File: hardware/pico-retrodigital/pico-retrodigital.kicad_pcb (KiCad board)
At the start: 2 copper layers, 50 x 38 mm, 70 parts, among them J1 Conn_02x05_Top_Bottom, J3 Conn_01x14, J4 Conn_01x02_Pin, J5 USB_C_Plug_USB2.0, U1 SN74LVC1G17DBVR, U2 SN74LVC1G17DBVR, U3 RP2354B, U4 SN74LVC245APW, U5 SN74LVC245APW, U6 SN74LVC245APW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

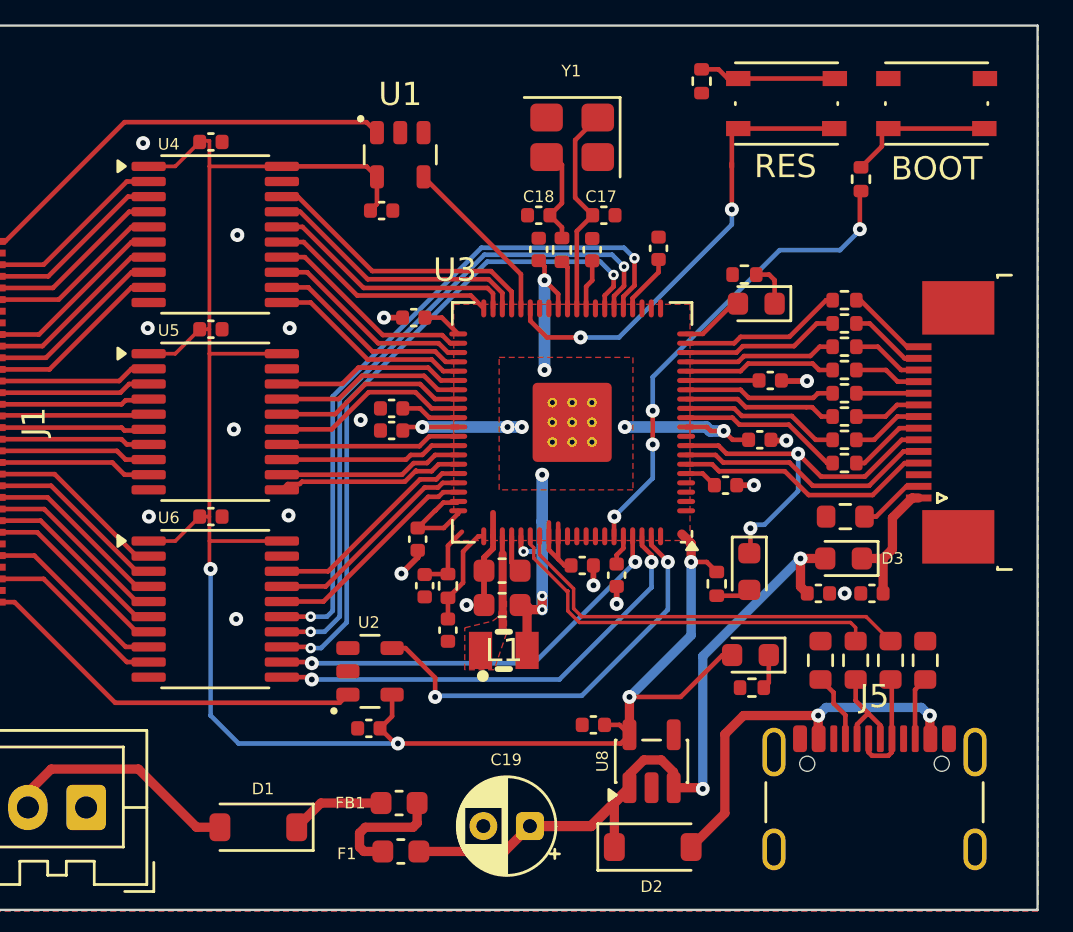
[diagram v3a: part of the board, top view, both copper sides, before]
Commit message: Clean up PCB DRC: thermal reliefs, via drills, small-via rule
- Bump all 0.6 mm vias to 0.3 mm drill (was 0.25); leave 9 small
  0.45/0.2 vias on +1V1 and CTL_0..2 untouched for tight routing
- Update Default netclass via_drill to 0.3
- Shrink thermal_bridge_width on both GND zones to 0.25 mm
- Switch U3 GND (pads 62, 81) and +1V1 (pads 10, 32, 51, 65) to
  solid zone connection for better grounding/heat dissipation
- Drop min_resolved_spokes from 2 to 1 (single-spoke thermals are
  electrically fine for reflow-assembled boards)
- Add .kicad_dru with a scoped exception allowing 0.45/0.2 vias only
  on +1V1, CTL_0, CTL_1, CTL_2 — other nets still require 0.5/0.3
- Ignore *_drc_violations.json (DRC runtime output)
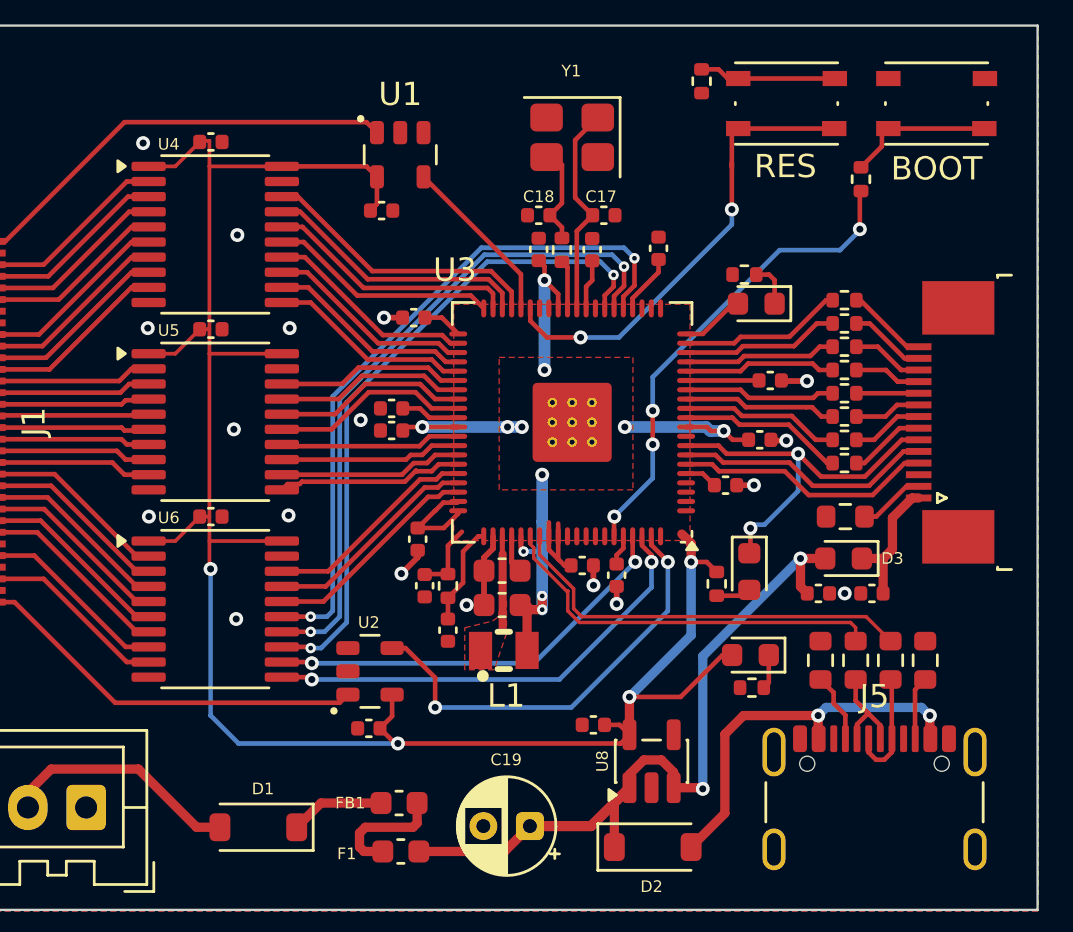
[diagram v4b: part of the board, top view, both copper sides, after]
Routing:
- net GND: track 10.3 -> 9.34 mm
- net AUD_CLK: track 18.2 -> 18.9 mm

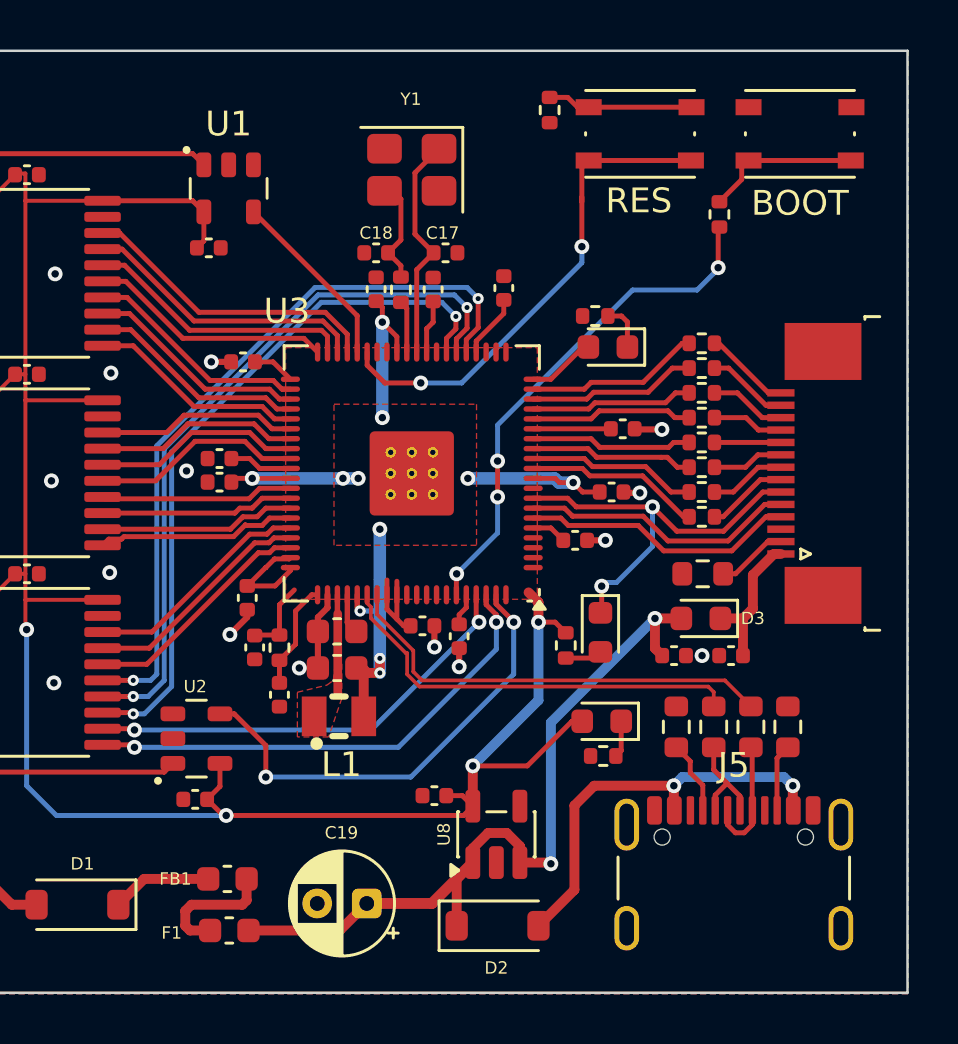
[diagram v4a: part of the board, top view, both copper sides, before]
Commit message: Refresh footprints from library; lower min silk text to 0.5 mm
- Pull current library copies for standard 0402/0603 R, C, D and FFC
  connector footprints (clears 29 of 36 lib_footprint_mismatch warnings
  and the 2 silk_over_copper)
- Drop min_text_height from 0.8 to 0.5 mm to match standard silk text
  on small SMD parts (clears 14 text_height warnings)
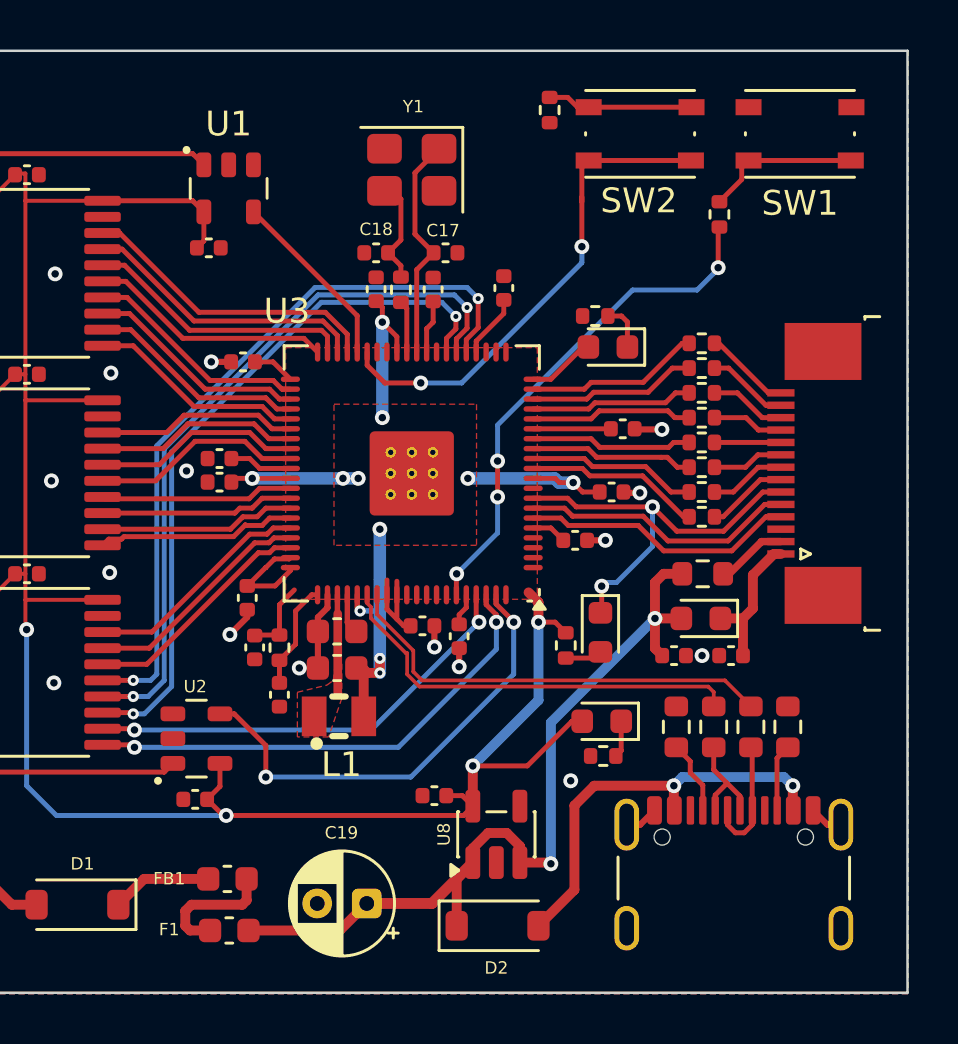
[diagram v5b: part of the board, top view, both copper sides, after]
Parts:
- renumbered BOOT to SW1, RES to SW2
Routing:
- net GND: track 9.34 -> 12.1 mm, vias 18 -> 19
- net +5V: track 32.2 -> 34.9 mm

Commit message: Update PCB
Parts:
- moved R11 2.31 mm to (84.7, 79.7)
- moved R13 2.01 mm to (77.3, 79.7)
- moved RES 0.90 mm to (80.8, 78.8)
- renumbered SW1 to BOOT, SW2 to RES
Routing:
- net Net-(U3-QSPI_SS): track 20.8 -> 23.0 mm
- net Net-(R11-Pad1): track 6.28 -> 5.72 mm
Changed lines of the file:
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@@
 		(descr "https://katalog.we-online.com/em/datasheet/434133025816.pdf")
 		(tags "tactile switch Wurth Wuerth")
-		(property "Reference" "SW1"
+		(property "Reference" "BOOT"
 			(at 0 2.8 0)
 			(layer "F.SilkS")
@@
 	(footprint "Resistor_SMD:R_0402_1005Metric"
 		(layer "F.Cu")
-		(at 78 77.84 90)
+		(at 77.35 79.74 90)
 		(descr "Resistor SMD 0402 (1005 Metric), square (rectangular) end terminal, IPC-7351 nominal, (Body size source: IPC-SM-782 page 72, https://www.pcb-3d.com/wordpress/wp-content/uploads/ipc-sm-782a_amendment_1_and_2.pdf)")
 		(tags "resistor")
@@
 	(footprint "Resistor_SMD:R_0402_1005Metric"
 		(layer "F.Cu")
-		(at 84.85 82.05 -90)
+		(at 84.7 79.74 -90)
 		(descr "Resistor SMD 0402 (1005 Metric), square (rectangular) end terminal, IPC-7351 nominal, (Body size source: IPC-SM-782 page 72, https://www.pcb-3d.com/wordpress/wp-content/uploads/ipc-sm-782a_amendment_1_and_2.pdf)")
 		(tags "resistor")
@@
 	(footprint "Button_Switch_SMD:SW_Push_1P1T_NO_Vertical_Wuerth_434133025816"
 		(layer "F.Cu")
-		(at 81.65 78.8)
+		(at 80.75 78.8)
 		(descr "https://katalog.we-online.com/em/datasheet/434133025816.pdf")
 		(tags "tactile switch Wurth Wuerth")
-		(property "Reference" "SW2"
+		(property "Reference" "RES"
 			(at -0.05 2.7 0)
 			(layer "F.SilkS")
@@
 	)
 	(segment
-		(start 84.85 81.54)
-		(end 85.75 80.64)
-		(width 0.2)
-		(layer "F.Cu")
-		(net "Net-(R11-Pad1)")
-	)
-	(segment
-		(start 85.75 80.64)
-		(end 85.75 80.15)
+		(start 86.025 79.875)
+		(end 85.345 79.875)
 		(width 0.2)
 		(layer "F.Cu")
@@
 	)
 	(segment
-		(start 85.75 80.15)
-		(end 86.025 79.875)
+		(start 85.345 79.875)
+		(end 84.7 79.23)
 		(width 0.2)
 		(layer "F.Cu")
@@
 	)
 	(segment
-		(start 83.725 77.725)
-		(end 79.575 77.725)
+		(start 82.825 77.725)
+		(end 78.675 77.725)
 		(width 0.2)
 		(layer "F.Cu")
@@
 	)
 	(segment
-		(start 79.575 77.725)
-		(end 79.125 77.725)
+		(start 78.675 77.725)
+		(end 77.35 79.05)
 		(width 0.2)
 		(layer "F.Cu")
@@
 	)
 	(segment
-		(start 78.73 77.33)
-		(end 78 77.33)
-		(width 0.2)
-		(layer "F.Cu")
-		(net "Net-(R13-Pad2)")
-	)
-	(segment
-		(start 79.125 77.725)
-		(end 78.73 77.33)
+		(start 77.35 79.05)
+		(end 77.35 79.23)
 		(width 0.2)
 		(layer "F.Cu")
@@
 	)
 	(segment
-		(start 84.8 84.2)
-		(end 84.8 82.61)
-		(width 0.2)
-		(layer "F.Cu")
-		(net "Net-(U3-QSPI_SS)")
-	)
-	(segment
-		(start 84.8 82.61)
-		(end 84.85 82.56)
+		(start 84.7 80.25)
+		(end 84.7 83.35)
 		(width 0.2)
 		(layer "F.Cu")
@@
 	)
 	(via
-		(at 84.8 84.2)
+		(at 84.7 83.35)
 		(size 0.6)
 		(drill 0.3)
@@
 	)
 	(segment
-		(start 75.9 90.55)
-		(end 75.9 92)
+		(start 84.65 84.4)
+		(end 83.95 85.1)
 		(width 0.2)
 		(layer "B.Cu")
@@
 	)
 	(segment
-		(start 84.8 84.2)
-		(end 84.65 84.35)
+		(start 75.9 90.55)
+		(end 75.9 92)
 		(width 0.2)
 		(layer "B.Cu")
@@
 	)
 	(segment
-		(start 84.65 84.4)
-		(end 83.95 85.1)
+		(start 84.7 83.35)
+		(end 84.65 83.4)
 		(width 0.2)
 		(layer "B.Cu")
@@
 	)
 	(segment
-		(start 74.25 96.55)
-		(end 75.9 94.9)
+		(start 84.65 83.4)
+		(end 84.65 84.4)
 		(width 0.2)
 		(layer "B.Cu")
@@
 	)
 	(segment
-		(start 84.65 84.35)
-		(end 84.65 84.4)
+		(start 74.25 96.55)
+		(end 75.9 94.9)
 		(width 0.2)
 		(layer "B.Cu")
@@
 	)
 	(segment
-		(start 81.35 85.1)
-		(end 75.9 90.55)
+		(start 75.9 94.9)
+		(end 75.9 93.45)
 		(width 0.2)
 		(layer "B.Cu")
@@
 	)
 	(segment
-		(start 75.9 94.9)
-		(end 75.9 93.45)
+		(start 81.35 85.1)
+		(end 75.9 90.55)
 		(width 0.2)
 		(layer "B.Cu")
@@
 	)
 	(segment
-		(start 72.8 88.85)
-		(end 71.35 88.85)
+		(start 78.675 79.875)
+		(end 78.675 83.425)
 		(width 0.2)
 		(layer "F.Cu")
@@
 	)
 	(segment
-		(start 79.575 79.875)
-		(end 83.7 79.875)
+		(start 72.8 88.85)
+		(end 71.35 88.85)
 		(width 0.2)
 		(layer "F.Cu")
@@
 	)
 	(segment
-		(start 70.6375 88.1375)
-		(end 70.6375 87.603)
+		(start 78.65 83.4)
+		(end 78.7 83.45)
 		(width 0.2)
 		(layer "F.Cu")
@@
 	)
 	(segment
-		(start 79.3 81.54)
-		(end 79.3 80.15)
+		(start 70.6375 88.1375)
+		(end 70.6375 87.603)
 		(width 0.2)
 		(layer "F.Cu")
@@
 	)
 	(segment
-		(start 79.3 80.15)
-		(end 79.575 79.875)
+		(start 78.675 79.875)
+		(end 82.8 79.875)
 		(width 0.2)
 		(layer "F.Cu")
@@
 	)
 	(segment
-		(start 79.3 81.35)
-		(end 79.3 83.35)
+		(start 78.675 83.425)
+		(end 78.7 83.45)
 		(width 0.2)
 		(layer "F.Cu")
@@
 	)
 	(via
-		(at 79.3 83.35)
+		(at 78.7 83.45)
 		(size 0.6)
 		(drill 0.3)
@@
 	)
 	(segment
-		(start 72.8 88.85)
+		(start 78.7 84.6)
 		(end 74.45 88.85)
 		(width 0.2)
@@
 	)
 	(segment
-		(start 74.45 88.85)
-		(end 79.3 84)
+		(start 78.7 83.45)
+		(end 78.7 84.6)
 		(width 0.2)
 		(layer "B.Cu")
@@
 	)
 	(segment
-		(start 79.3 84)
-		(end 79.3 83.35)
+		(start 74.45 88.85)
+		(end 72.8 88.85)
 		(width 0.2)
 		(layer "B.Cu")
